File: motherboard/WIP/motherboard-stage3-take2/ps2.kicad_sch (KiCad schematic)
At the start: 24 parts, among them U1 74HCT32, U2 74HCT14, U3 74HCT595, U4 74HCT595, U5 74HCT14, U6 74HCT573, U7 74HCT595, U8 74HCT595, U9 74HCT573

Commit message: Ordered stage 2!
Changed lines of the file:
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@@
+	(wire
+		(pts
+			(xy 254 77.47) (xy 255.27 77.47)
+		)
+		(stroke
+			(width 0)
+			(type default)
+		)
+	)
 	(wire
 		(pts
@@
 	)
 	(hierarchical_label "~{INT_PS2_KB}"
-		(shape input)
-		(at 254 77.47 0)
-		(fields_autoplaced yes)
-		(effects
+		(shape output)
+		(at 255.27 77.47 0)
+		(fields_autoplaced yes)
+		(effects

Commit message: Updated stage 2 and stage 3, and started on a cf addon
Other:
- company: (none) -> Eric Lind
- title: (none) -> MicroLind - PS2 interface, Mouse & Kbd
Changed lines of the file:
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@@
 	(generator_version "8.0")
 	(paper "A4")
+	(title_block
+		(title "MicroLind - PS2 interface, Mouse & Kbd")
+		(date "2025-03-03")
+		(rev "C0")
+		(company "Eric Lind")
+	)
 	(junction
 		(at 80.01 27.94)

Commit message: Updates
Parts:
- U33: renamed from U6; value 74HCT573 -> 74HCT574
- U36: renamed from U9; value 74HCT573 -> 74HCT574
- renumbered C1 to C36, C2 to C42, C3 to C43, C4 to C44, C5 to C45, C6 to C46, C7 to C47, C8 to C48, C9 to C49, C10 to C50, J1 to P9, R1 to R13, R2 to R14, R3 to R15, R4 to R16, U1 to U29, U5 to U30, U3 to U31, U4 to U32, U7 to U34, U8 to U35, U2 to U9

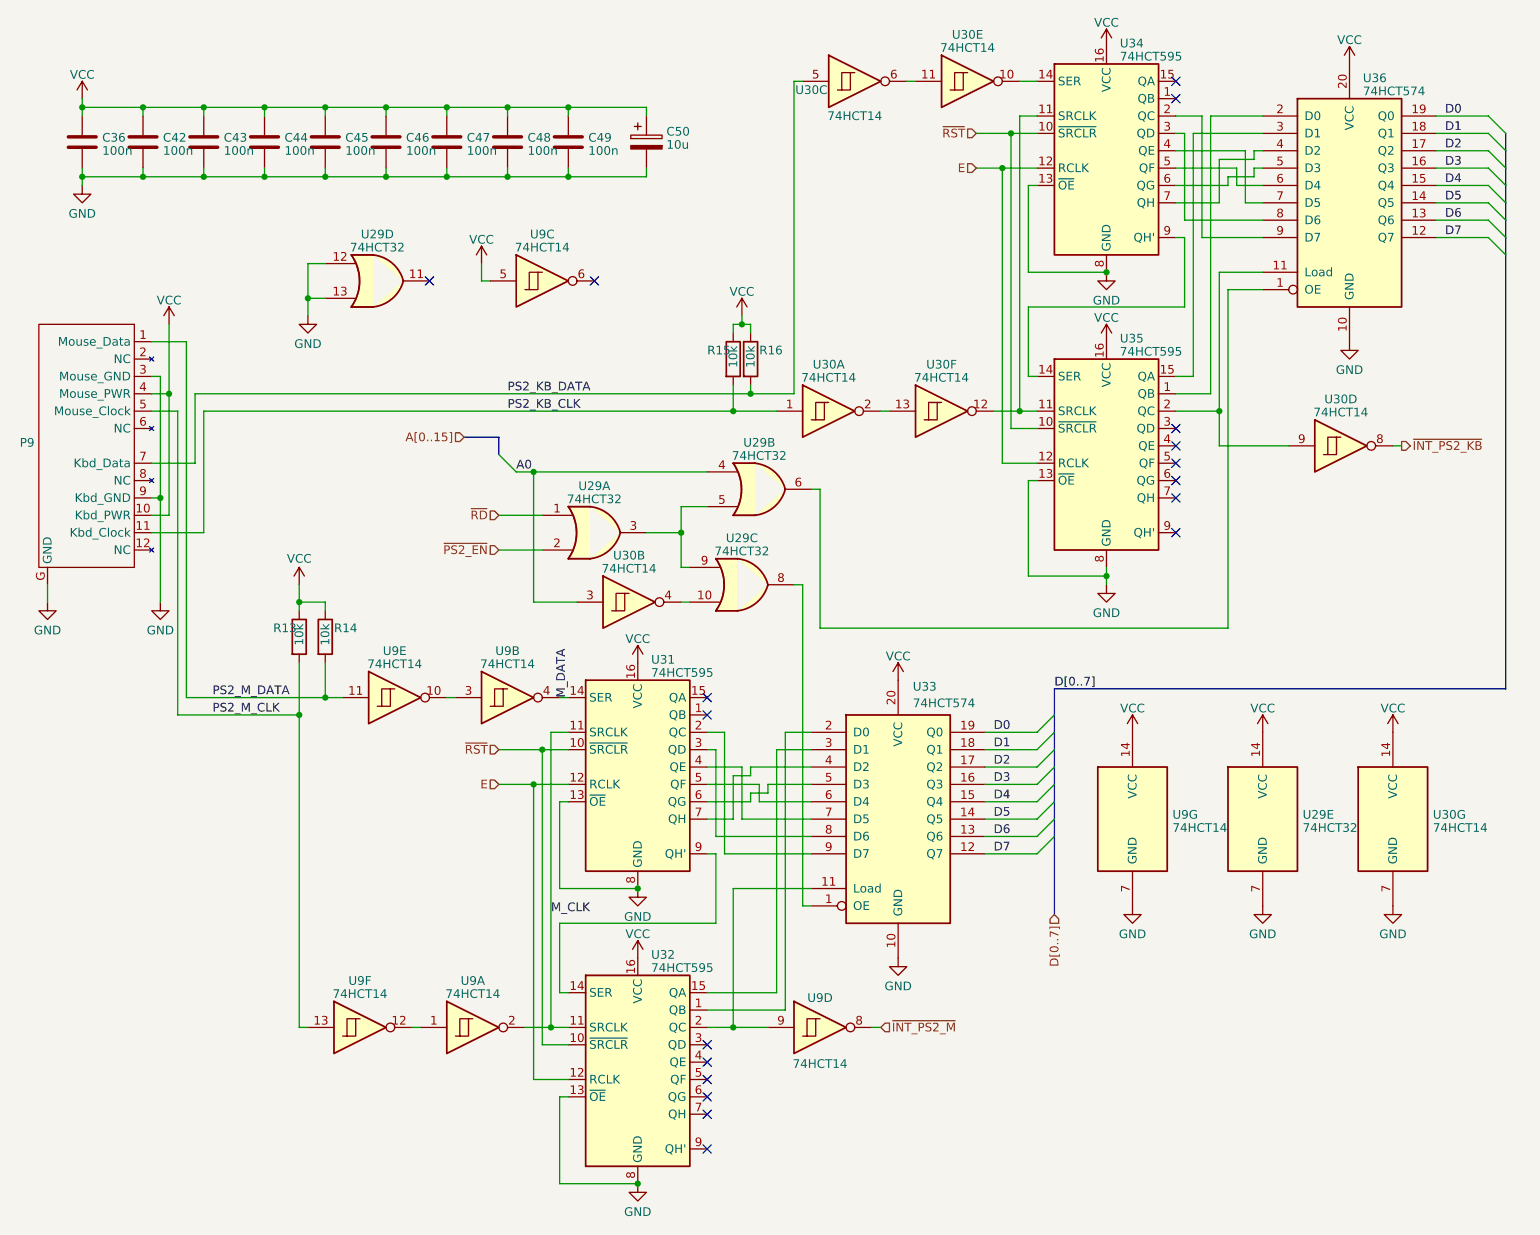
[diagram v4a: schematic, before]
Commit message: Updated stage 3 with ps2 fix, added warning to PS/2 proto
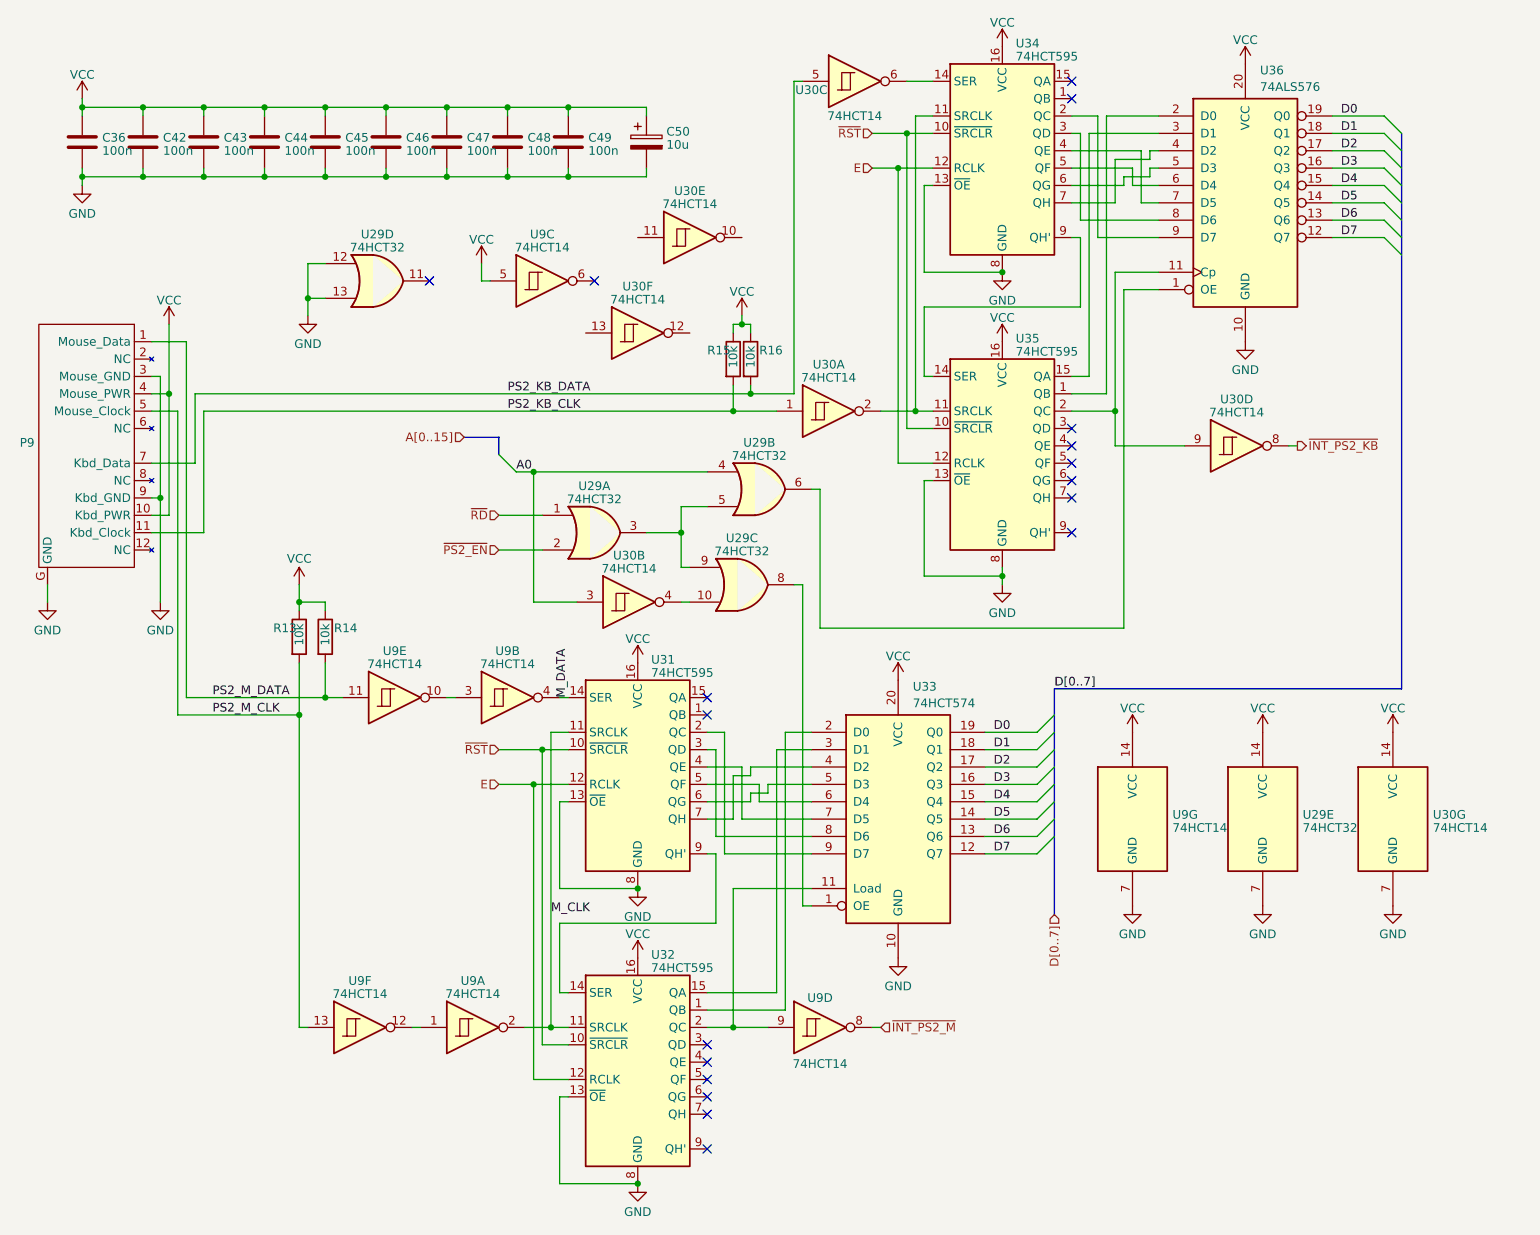
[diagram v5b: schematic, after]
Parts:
- removed U36: 74HCT574, Package_DIP:DIP-20_W7.62mm_Socket, symbol 74xx:74LS573
- added U36: 74ALS576, Package_DIP:DIP-20_W7.62mm_Socket, symbol microlind:74ALS576
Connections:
- net D0: now also U36.19 (Q0)
- net D1: now also U36.18 (Q1)
- net D2: now also U36.17 (Q2)
- net D3: now also U36.16 (Q3)
- net D4: now also U36.15 (Q4)
- net D5: now also U36.14 (Q5)
- net D6: now also U36.13 (Q6)
- net D7: now also U36.12 (Q7)
- net GND: now also U36.10 (GND)
- net VCC: now also U36.20 (VCC)
- net at U29.6: now also U36.1 (OE)
- net at U30.10: no longer U34.14 (SER)
- net at U30.11: no longer U30.6
- net at U30.2: now also U34.11 (SRCLK), U35.11 (SRCLK); no longer U30.13
- net at U35.1 (QB): now also U36.2 (D0)
- net at U35.15 (QA): now also U36.3 (D1)
- net at U30.9, U35.2 (QC): now also U36.11 (Cp)
- net at U34.7 (QH): now also U36.4 (D2)
- net at U34.6 (QG): now also U36.5 (D3)
- net at U34.5 (QF): now also U36.6 (D4)
- net at U34.4 (QE): now also U36.7 (D5)
- net at U34.3 (QD): now also U36.8 (D6)
- net at U34.2 (QC): now also U36.9 (D7)
- new net: U30.6, U34.14 (SER)
- now unconnected: U30.12
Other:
- moved on the sheet: U30D, U30E, U30F, U34, U35

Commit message: Added new ps handling in stage3-rev1
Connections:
- net M_CLK: now also U9.4; no longer U9.2
- net M_DATA: now also U9.12; no longer U9.4
- net PS2_KB_DATA: now also U30.11; no longer U30.5
- net PS2_M_CLK: now also U9.1; no longer U9.13
- net PS2_M_DATA: now also U9.13; no longer U9.11
- net VCC: now also U30.13, U9.11
- net at U29.8, U33.1 (OE): now also U31.10 (~{SRCLR}), U32.10 (~{SRCLR})
- net at U29.6, U36.1 (OE): now also U34.10 (~{SRCLR}), U35.10 (~{SRCLR})
- net at U30.10: now also U34.14 (SER)
- net at U9.3: now also U9.2; no longer U9.10
- net at U34.11 (SRCLK), U35.11 (SRCLK): now also U30.6; no longer U30.2
- removed net ~{RST}: U31.10 (~{SRCLR}), U32.10 (~{SRCLR}), U34.10 (~{SRCLR}), U35.10 (~{SRCLR})
- new net: U30.2, U30.5
- no-connect marks 18 -> 20
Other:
- moved on the sheet: U30C, U30D, U30E, U30F, U34, U35, U36, U9A, U9B, U9E, U9F
